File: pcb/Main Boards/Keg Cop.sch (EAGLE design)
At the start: 14 parts, among them X1 RJ45-8X, X2 RJ45-8X

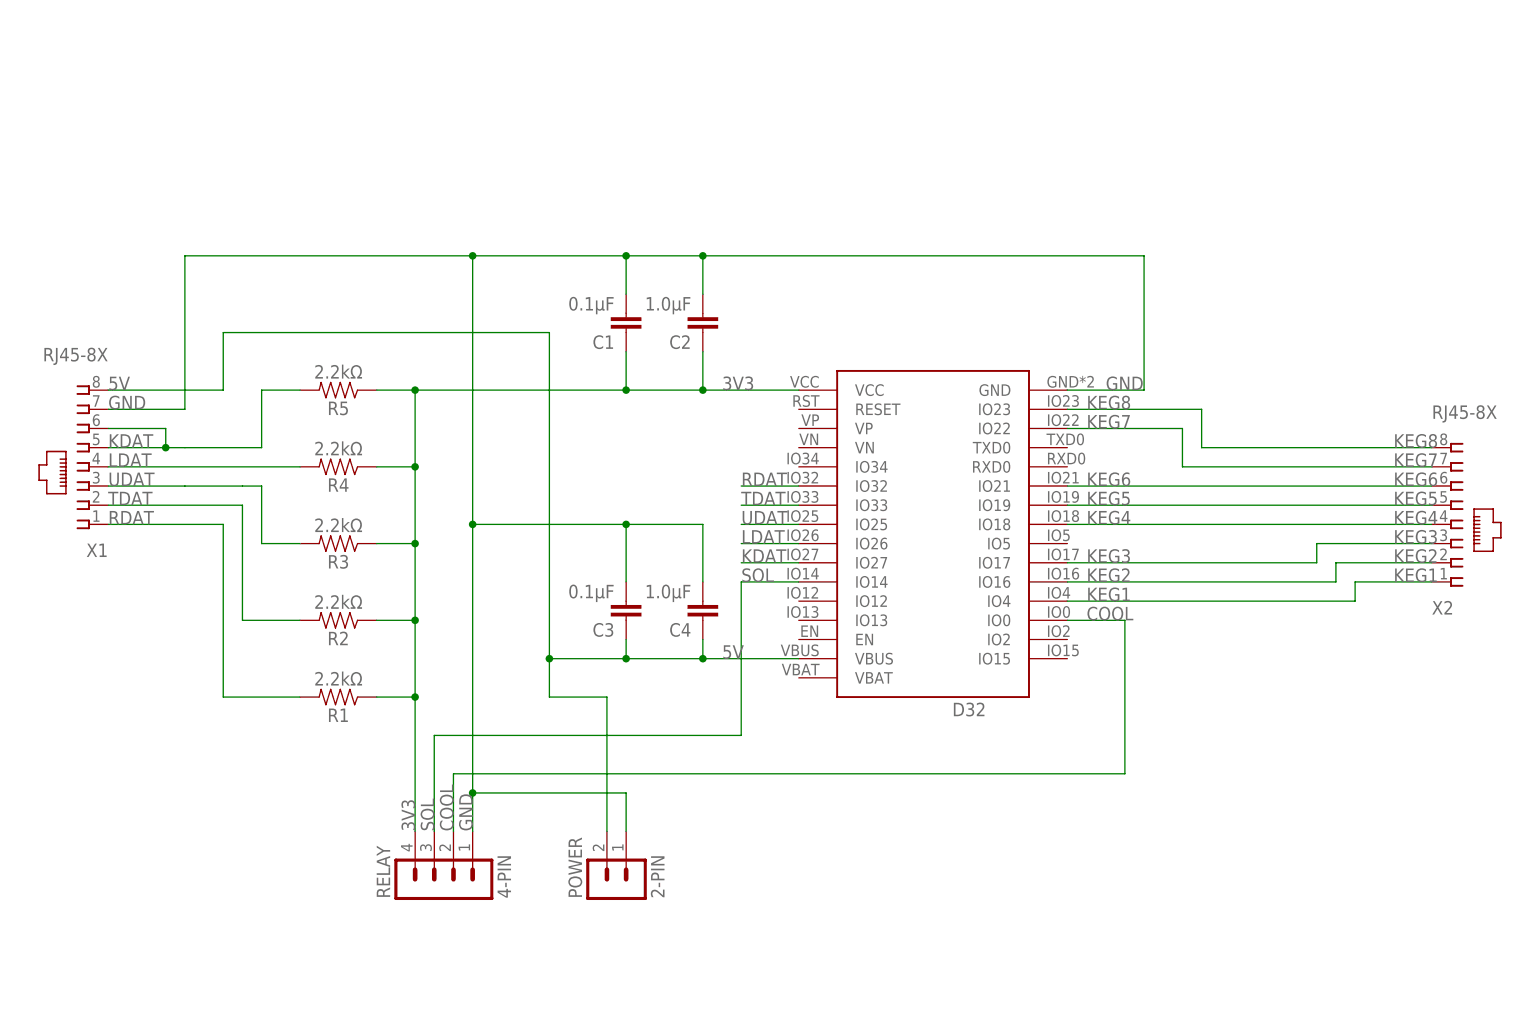
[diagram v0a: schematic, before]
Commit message: Swap pins, split dirs
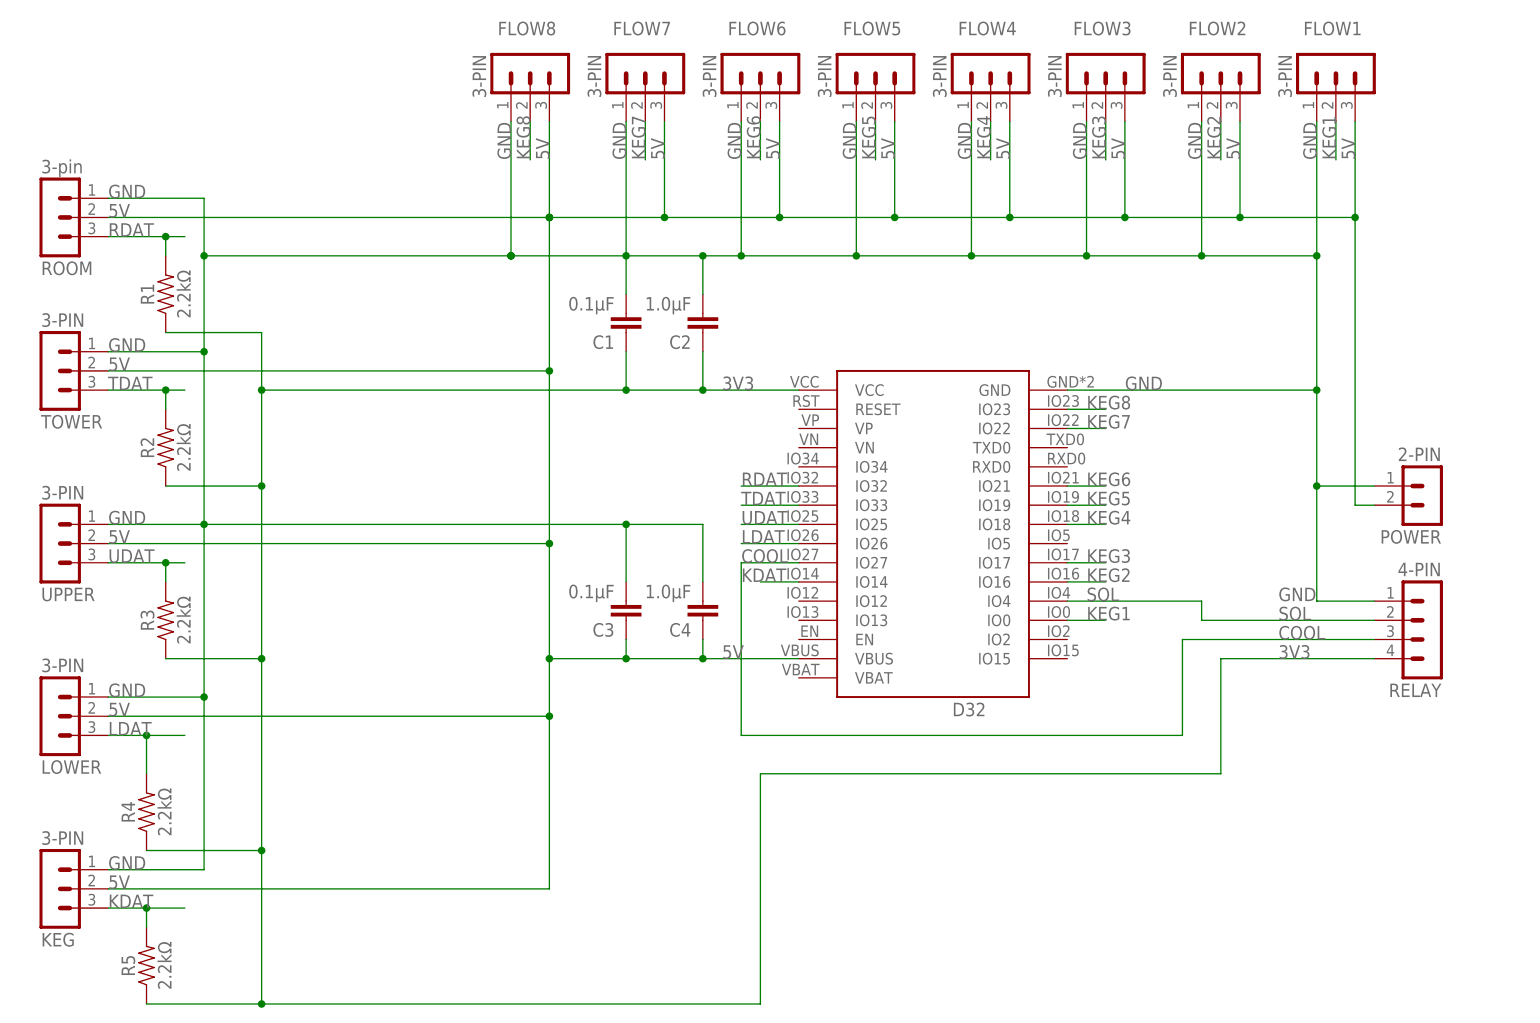
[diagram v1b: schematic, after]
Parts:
- removed X1, X2: RJ45-8X, con-tycoelectronics:RJ45-8X
- added FLOW1, FLOW2, FLOW3, FLOW4, FLOW5, FLOW6, FLOW7, FLOW8, KEG, LOWER, TOWER, UPPER: 3-PIN, Donnie:MA03-1
- added ROOM: 3-pin, Donnie:MA03-1
- D32: value Lolin D32 -> U1
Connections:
- net 5V: now also FLOW1.3, FLOW2.3, FLOW3.3, FLOW4.3, FLOW5.3, FLOW6.3, FLOW7.3, FLOW8.3, KEG.2, LOWER.2, ROOM.2, TOWER.2, UPPER.2; no longer X1.8
- net COOL: now also D32.IO27, RELAY.3; no longer D32.IO0, RELAY.2
- net GND: now also FLOW1.1, FLOW2.1, FLOW3.1, FLOW4.1, FLOW5.1, FLOW6.1, FLOW7.1, FLOW8.1, KEG.1, LOWER.1, ROOM.1, TOWER.1, UPPER.1; no longer X1.7
- net KDAT: now also D32.IO14, KEG.3; no longer D32.IO27, X1.5, X1.6
- net KEG1: now also D32.IO0, FLOW1.2; no longer D32.IO4, X2.1
- net KEG2: now also FLOW2.2; no longer X2.2
- net KEG3: now also FLOW3.2; no longer X2.3
- net KEG4: now also FLOW4.2; no longer X2.4
- net KEG5: now also FLOW5.2; no longer X2.5
- net KEG6: now also FLOW6.2; no longer X2.6
- net KEG7: now also FLOW7.2; no longer X2.7
- net KEG8: now also FLOW8.2; no longer X2.8
- net LDAT: now also LOWER.3; no longer X1.4
- net RDAT: now also ROOM.3; no longer X1.1
- net SOL: now also D32.IO4, RELAY.2; no longer D32.IO14, RELAY.3
- net TDAT: now also TOWER.3; no longer X1.2
- net UDAT: now also UPPER.3; no longer X1.3
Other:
- moved on the sheet: POWER, R1, R2, R3, R4, R5, RELAY
